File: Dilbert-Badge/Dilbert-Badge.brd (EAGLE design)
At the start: 100 x 80 mm, 5 parts

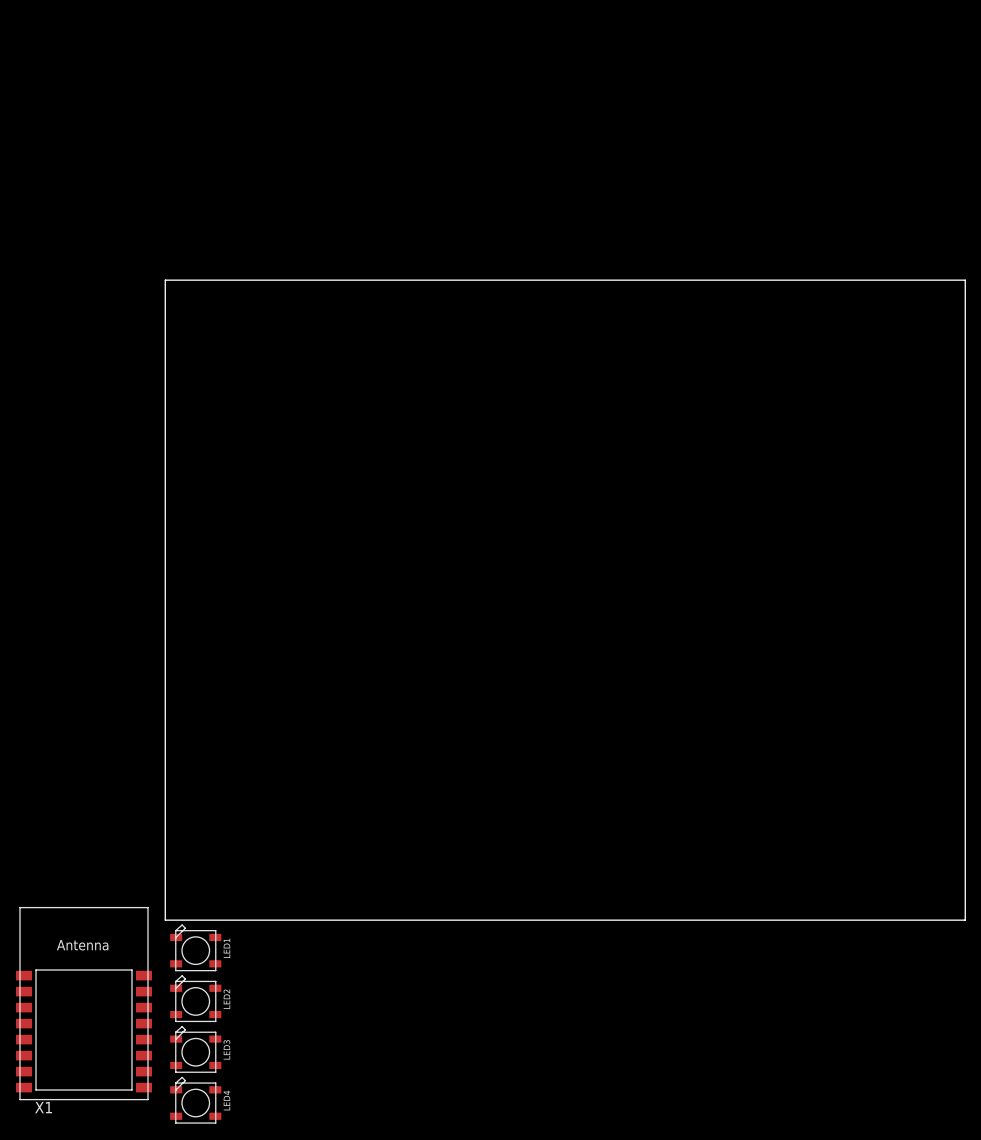
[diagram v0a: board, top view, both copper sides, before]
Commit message: add switches, initial layout
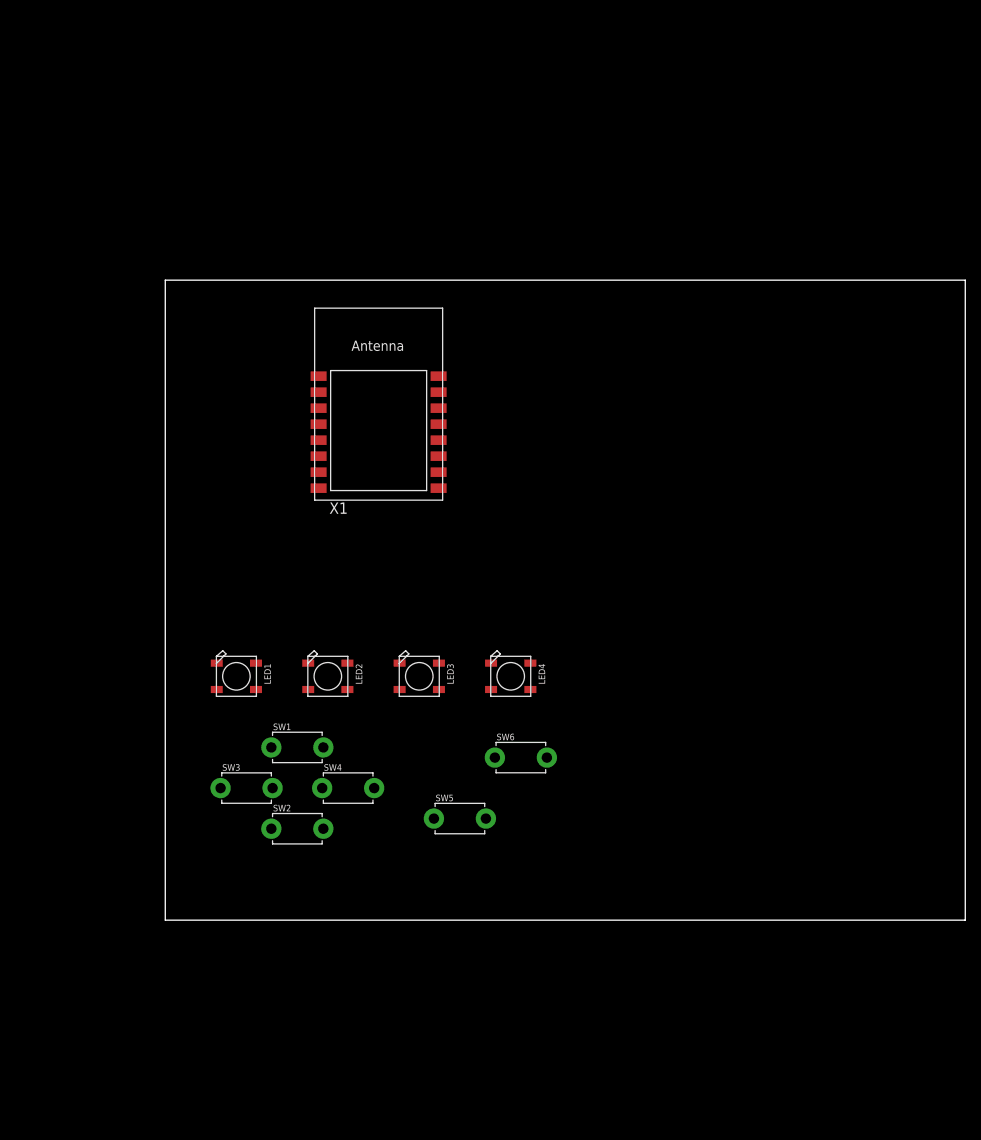
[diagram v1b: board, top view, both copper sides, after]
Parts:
- added SW1: UP, adafruit:TACT_PANA-EVQ
- added SW2: DOWN, adafruit:TACT_PANA-EVQ
- added SW3: LEFT, adafruit:TACT_PANA-EVQ
- added SW4: RIGHT, adafruit:TACT_PANA-EVQ
- added SW5: A, adafruit:TACT_PANA-EVQ
- added SW6: B, adafruit:TACT_PANA-EVQ
- moved X1 83.5 mm to (26.7, 63.5)
- moved LED4 66.3 mm to (43.2, 30.5)
- moved LED3 54.7 mm to (31.8, 30.5)
- moved LED2 43.9 mm to (20.3, 30.5)
- moved LED1 34.7 mm to (8.89, 30.5)
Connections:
- net VCC renamed N$4
- removed net N$6: LED1.3-GND, LED2.3-GND, LED3.3-GND, LED4.3-GND
- new net BTN_A: SW5.P$2
- new net BTN_B: SW6.P$2
- new net BTN_D: SW2.P$2
- new net BTN_L: SW3.P$2
- new net BTN_R: SW4.P$2
- new net BTN_U: SW1.P$2
- net GND: now also LED1.3-GND, LED2.3-GND, LED3.3-GND, LED4.3-GND, SW1.P$1, SW4.P$1, SW5.P$1, SW6.P$1
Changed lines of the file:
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@@
 </autorouter>
 <elements>
-<element name="LED1" library="adafruit" package="WS2812B" value="WS2812B5050" x="3.81" y="-3.81"/>
-<element name="LED2" library="adafruit" package="WS2812B" value="WS2812B5050" x="3.81" y="-10.16"/>
-<element name="LED3" library="adafruit" package="WS2812B" value="WS2812B5050" x="3.81" y="-16.51"/>
-<element name="LED4" library="adafruit" package="WS2812B" value="WS2812B5050" x="3.81" y="-22.86"/>
-<element name="X1" library="adafruit" package="ESP-12" value="" x="-10.16" y="-11.43"/>
+<element name="LED1" library="adafruit" package="WS2812B" value="WS2812B5050" x="8.89" y="30.48"/>
+<element name="LED2" library="adafruit" package="WS2812B" value="WS2812B5050" x="20.32" y="30.48"/>
+<element name="LED3" library="adafruit" package="WS2812B" value="WS2812B5050" x="31.75" y="30.48"/>
+<element name="LED4" library="adafruit" package="WS2812B" value="WS2812B5050" x="43.18" y="30.48"/>
+<element name="X1" library="adafruit" package="ESP-12" value="" x="26.67" y="63.5"/>
+<element name="SW1" library="adafruit" package="TACT_PANA-EVQ" value="UP" x="16.51" y="21.59"/>
+<element name="SW2" library="adafruit" package="TACT_PANA-EVQ" value="DOWN" x="16.51" y="11.43"/>
+<element name="SW3" library="adafruit" package="TACT_PANA-EVQ" value="LEFT" x="10.16" y="16.51"/>
+<element name="SW4" library="adafruit" package="TACT_PANA-EVQ" value="RIGHT" x="22.86" y="16.51"/>
+<element name="SW5" library="adafruit" package="TACT_PANA-EVQ" value="A" x="36.83" y="12.7"/>
+<element name="SW6" library="adafruit" package="TACT_PANA-EVQ" value="B" x="44.45" y="20.32"/>
 </elements>
 <signals>
@@
 <contactref element="LED1" pad="2-DOUT"/>
 <contactref element="LED2" pad="4-DIN"/>
-<wire x1="6.26" y1="-2.16" x2="1.36" y2="-11.81" width="0" layer="19" extent="1-1"/>
+<wire x1="11.34" y1="32.13" x2="17.87" y2="28.83" width="0" layer="19" extent="1-1"/>
 </signal>
 <signal name="N$2">
 <contactref element="LED2" pad="2-DOUT"/>
 <contactref element="LED3" pad="4-DIN"/>
-<wire x1="6.26" y1="-8.51" x2="1.36" y2="-18.16" width="0" layer="19" extent="1-1"/>
+<wire x1="22.77" y1="32.13" x2="29.3" y2="28.83" width="0" layer="19" extent="1-1"/>
 </signal>
 <signal name="N$3">
 <contactref element="LED3" pad="2-DOUT"/>
 <contactref element="LED4" pad="4-DIN"/>
-<wire x1="6.26" y1="-14.86" x2="1.36" y2="-24.51" width="0" layer="19" extent="1-1"/>
+<wire x1="34.2" y1="32.13" x2="40.73" y2="28.83" width="0" layer="19" extent="1-1"/>
 </signal>
 <signal name="N$5">
@@
 <contactref element="LED1" pad="1-VDD"/>
 <contactref element="LED2" pad="1-VDD"/>
-<wire x1="6.26" y1="-18.16" x2="6.26" y2="-24.51" width="0" layer="19" extent="1-1"/>
-<wire x1="6.26" y1="-11.81" x2="6.26" y2="-18.16" width="0" layer="19" extent="1-1"/>
-<wire x1="6.26" y1="-5.46" x2="6.26" y2="-11.81" width="0" layer="19" extent="1-1"/>
+<wire x1="34.2" y1="28.83" x2="45.63" y2="28.83" width="0" layer="19" extent="1-1"/>
+<wire x1="22.77" y1="28.83" x2="34.2" y2="28.83" width="0" layer="19" extent="1-1"/>
+<wire x1="11.34" y1="28.83" x2="22.77" y2="28.83" width="0" layer="19" extent="1-1"/>
 </signal>
-<signal name="N$6">
+<signal name="GND">
+<contactref element="SW1" pad="P$1"/>
+<contactref element="SW4" pad="P$1"/>
+<contactref element="SW5" pad="P$1"/>
+<contactref element="SW6" pad="P$1"/>
 <contactref element="LED1" pad="3-GND"/>
 <contactref element="LED2" pad="3-GND"/>
 <contactref element="LED3" pad="3-GND"/>
 <contactref element="LED4" pad="3-GND"/>
-<wire x1="1.36" y1="-14.86" x2="1.36" y2="-21.21" width="0" layer="19" extent="1-1"/>
-<wire x1="1.36" y1="-8.51" x2="1.36" y2="-14.86" width="0" layer="19" extent="1-1"/>
-<wire x1="1.36" y1="-2.16" x2="1.36" y2="-8.51" width="0" layer="19" extent="1-1"/>
+<contactref element="X1" pad="9"/>
+<wire x1="33.58" y1="12.7" x2="41.2" y2="20.32" width="0" layer="19" extent="1-1"/>
+<wire x1="19.61" y1="16.51" x2="33.58" y2="12.7" width="0" layer="19" extent="1-1"/>
+<wire x1="13.26" y1="21.59" x2="19.61" y2="16.51" width="0" layer="19" extent="1-1"/>
+<wire x1="34.17" y1="54" x2="13.26" y2="21.59" width="0" layer="19" extent="1-1"/>
+<wire x1="40.73" y1="32.13" x2="34.17" y2="54" width="0" layer="19" extent="1-1"/>
+<wire x1="29.3" y1="32.13" x2="40.73" y2="32.13" width="0" layer="19" extent="1-1"/>
+<wire x1="17.87" y1="32.13" x2="29.3" y2="32.13" width="0" layer="19" extent="1-1"/>
+<wire x1="6.44" y1="32.13" x2="17.87" y2="32.13" width="0" layer="19" extent="1-1"/>
 </signal>
-<signal name="VCC">
+<signal name="BTN_U">
+<contactref element="SW1" pad="P$2"/>
+</signal>
+<signal name="BTN_D">
+<contactref element="SW2" pad="P$2"/>
+</signal>
+<signal name="BTN_L">
+<contactref element="SW3" pad="P$2"/>
+</signal>
+<signal name="BTN_R">
+<contactref element="SW4" pad="P$2"/>
+</signal>
+<signal name="BTN_A">
+<contactref element="SW5" pad="P$2"/>
+</signal>
+<signal name="BTN_B">
+<contactref element="SW6" pad="P$2"/>
+</signal>
+<signal name="N$4">
 <contactref element="X1" pad="8"/>
 </signal>
-<signal name="GND">
-<contactref element="X1" pad="9"/>
-</signal>
 </signals>

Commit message: a little more work
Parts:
- added J1: I2C, SparkFun-Connectors:1X04
- added J2: UART, SparkFun-Connectors:1X06
- added J3: (no value), SparkFun-Connectors:1X03
- added J4, J5: (no value), SparkFun-Connectors:1X08_NO_SILK
- added SW7: RESET, adafruit:TACT_PANA-EVQ
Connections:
- new net LED_IN: J5.7, LED1.4-DIN, X1.10
- new net LED_OUT: J3.3, LED4.2-DOUT
- new net N$10: J4.2, X1.7
- new net N$11: J4.3, X1.6
- new net N$12: J5.3, X1.14
- new net N$13: J5.6, X1.11
- new net N$6: J4.6, X1.3
- new net N$7: J4.5, X1.4
- new net N$8: J4.8, X1.1
- new net N$9: J4.4, X1.5
- new net SCL: J1.4, J5.5, X1.12
- new net SDA: J1.3, J5.4, X1.13
- new net UART_CTS: J2.5
- new net UART_DTR: J2.1
- new net UART_RX: J2.3, J5.2, X1.15
- new net UART_TX: J2.2, J5.1, X1.16
- new net VCC: J1.2, J2.4, J3.2, J4.1, X1.8
- net GND: now also J1.1, J2.6, J3.1, J5.8, SW2.P$1, SW3.P$1, SW7.P$1
- net N$4: now also J4.7, X1.2; no longer X1.8
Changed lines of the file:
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@@
 <setting verticaltext="up"/>
 </settings>
-<grid distance="0.05" unitdist="inch" unit="inch" style="lines" multiple="1" display="no" altdistance="0.025" altunitdist="inch" altunit="inch"/>
+<grid distance="0.05" unitdist="inch" unit="inch" style="lines" multiple="1" display="yes" altdistance="0.025" altunitdist="inch" altunit="inch"/>
 <layers>
 <layer number="1" name="Top" color="4" fill="1" visible="yes" active="yes"/>
@@
 <layer number="112" name="tSilk" color="7" fill="1" visible="no" active="yes"/>
 <layer number="113" name="ReferenceLS" color="7" fill="1" visible="no" active="no"/>
+<layer number="114" name="Badge_Outline" color="7" fill="1" visible="yes" active="yes"/>
+<layer number="115" name="ReferenceISLANDS" color="7" fill="1" visible="yes" active="yes"/>
 <layer number="116" name="Patch_BOT" color="9" fill="4" visible="no" active="yes"/>
 <layer number="118" name="Rect_Pads" color="7" fill="1" visible="no" active="no"/>
@@
 <element name="SW5" library="adafruit" package="TACT_PANA-EVQ" value="A" x="36.83" y="12.7"/>
 <element name="SW6" library="adafruit" package="TACT_PANA-EVQ" value="B" x="44.45" y="20.32"/>
+<element name="J1" library="SparkFun-Connectors" package="1X04" value="I2C" x="2.54" y="-3.81">
+<attribute name="PROD_ID" value="CONN-09696" x="2.54" y="-3.81" size="1.778" layer="27" display="off"/>
+</element>
+<element name="J2" library="SparkFun-Connectors" package="1X06" value="UART" x="2.54" y="-8.89">
+<attribute name="PROD_ID" value="CONN-08437" x="2.54" y="-8.89" size="1.778" layer="27" display="off"/>
+</element>
+<element name="J3" library="SparkFun-Connectors" package="1X03" value="" x="2.54" y="-16.51"/>
+<element name="J4" library="SparkFun-Connectors" package="1X08_NO_SILK" value="" x="15.24" y="53.34" rot="R90">
+<attribute name="PROD_ID" value="CONN-08438" x="15.24" y="53.34" size="1.778" layer="27" rot="R90" display="off"/>
+</element>
+<element name="J5" library="SparkFun-Connectors" package="1X08_NO_SILK" value="" x="38.1" y="71.12" rot="R270">
+<attribute name="PROD_ID" value="CONN-08438" x="38.1" y="71.12" size="1.778" layer="27" rot="R270" display="off"/>
+</element>
+<element name="SW7" library="adafruit" package="TACT_PANA-EVQ" value="RESET" x="5.08" y="-21.59"/>
 </elements>
 <signals>
@@
 <contactref element="LED4" pad="3-GND"/>
 <contactref element="X1" pad="9"/>
-<wire x1="33.58" y1="12.7" x2="41.2" y2="20.32" width="0" layer="19" extent="1-1"/>
-<wire x1="19.61" y1="16.51" x2="33.58" y2="12.7" width="0" layer="19" extent="1-1"/>
-<wire x1="13.26" y1="21.59" x2="19.61" y2="16.51" width="0" layer="19" extent="1-1"/>
-<wire x1="34.17" y1="54" x2="13.26" y2="21.59" width="0" layer="19" extent="1-1"/>
-<wire x1="40.73" y1="32.13" x2="34.17" y2="54" width="0" layer="19" extent="1-1"/>
+<contactref element="J2" pad="6"/>
+<contactref element="J1" pad="1"/>
+<contactref element="J3" pad="1"/>
+<contactref element="SW2" pad="P$1"/>
+<contactref element="SW3" pad="P$1"/>
+<contactref element="J5" pad="8"/>
+<contactref element="SW7" pad="P$1"/>
+<wire x1="34.17" y1="54" x2="38.1" y2="53.34" width="0" layer="19" extent="1-1"/>
+<wire x1="40.73" y1="32.13" x2="38.1" y2="53.34" width="0" layer="19" extent="1-1"/>
 <wire x1="29.3" y1="32.13" x2="40.73" y2="32.13" width="0" layer="19" extent="1-1"/>
 <wire x1="17.87" y1="32.13" x2="29.3" y2="32.13" width="0" layer="19" extent="1-1"/>
 <wire x1="6.44" y1="32.13" x2="17.87" y2="32.13" width="0" layer="19" extent="1-1"/>
+<wire x1="13.26" y1="21.59" x2="17.87" y2="32.13" width="0" layer="19" extent="1-1"/>
+<wire x1="19.61" y1="16.51" x2="13.26" y2="21.59" width="0" layer="19" extent="1-1"/>
+<wire x1="13.26" y1="11.43" x2="19.61" y2="16.51" width="0" layer="19" extent="1-1"/>
+<wire x1="6.91" y1="16.51" x2="13.26" y2="21.59" width="0" layer="19" extent="1-1"/>
+<wire x1="41.2" y1="20.32" x2="40.73" y2="32.13" width="0" layer="19" extent="1-1"/>
+<wire x1="33.58" y1="12.7" x2="41.2" y2="20.32" width="0" layer="19" extent="1-1"/>
+<wire x1="2.54" y1="-3.81" x2="13.26" y2="11.43" width="0" layer="19" extent="1-1"/>
+<wire x1="2.54" y1="-16.51" x2="2.54" y2="-3.81" width="0" layer="19" extent="1-1"/>
+<wire x1="1.83" y1="-21.59" x2="2.54" y2="-16.51" width="0" layer="19" extent="1-1"/>
+<wire x1="15.24" y1="-8.89" x2="2.54" y2="-3.81" width="0" layer="19" extent="1-1"/>
 </signal>
 <signal name="BTN_U">
@@
 <contactref element="SW6" pad="P$2"/>
 </signal>
+<signal name="N$8">
+<contactref element="X1" pad="1"/>
+<contactref element="J4" pad="8"/>
+<wire x1="15.24" y1="71.12" x2="19.17" y2="68" width="0" layer="19" extent="1-1"/>
+</signal>
+<signal name="SDA">
+<contactref element="X1" pad="13"/>
+<contactref element="J1" pad="3"/>
+<contactref element="J5" pad="4"/>
+<wire x1="7.62" y1="-3.81" x2="34.17" y2="62" width="0" layer="19" extent="1-1"/>
+<wire x1="38.1" y1="63.5" x2="7.62" y2="-3.81" width="0" layer="19" extent="1-1"/>
+</signal>
+<signal name="SCL">
+<contactref element="X1" pad="12"/>
+<contactref element="J1" pad="4"/>
+<contactref element="J5" pad="5"/>
+<wire x1="10.16" y1="-3.81" x2="34.17" y2="60" width="0" layer="19" extent="1-1"/>
+<wire x1="38.1" y1="60.96" x2="10.16" y2="-3.81" width="0" layer="19" extent="1-1"/>
+</signal>
+<signal name="UART_TX">
+<contactref element="X1" pad="16"/>
+<contactref element="J2" pad="2"/>
+<contactref element="J5" pad="1"/>
+<wire x1="5.08" y1="-8.89" x2="34.17" y2="68" width="0" layer="19" extent="1-1"/>
+<wire x1="38.1" y1="71.12" x2="5.08" y2="-8.89" width="0" layer="19" extent="1-1"/>
+</signal>
+<signal name="UART_RX">
+<contactref element="X1" pad="15"/>
+<contactref element="J2" pad="3"/>
+<contactref element="J5" pad="2"/>
+<wire x1="7.62" y1="-8.89" x2="34.17" y2="66" width="0" layer="19" extent="1-1"/>
+<wire x1="38.1" y1="68.58" x2="7.62" y2="-8.89" width="0" layer="19" extent="1-1"/>
+</signal>
+<signal name="UART_CTS">
+<contactref element="J2" pad="5"/>
+</signal>
+<signal name="VCC">
+<contactref element="J2" pad="4"/>
+<contactref element="X1" pad="8"/>
+<contactref element="J3" pad="2"/>
+<contactref element="J1" pad="2"/>
+<contactref element="J4" pad="1"/>
+<wire x1="5.08" y1="-3.81" x2="19.17" y2="54" width="0" layer="19" extent="1-1"/>
+<wire x1="10.16" y1="-8.89" x2="5.08" y2="-3.81" width="0" layer="19" extent="1-1"/>
+<wire x1="5.08" y1="-16.51" x2="10.16" y2="-8.89" width="0" layer="19" extent="1-1"/>
+<wire x1="15.24" y1="53.34" x2="5.08" y2="-16.51" width="0" layer="19" extent="1-1"/>
+</signal>
+<signal name="UART_DTR">
+<contactref element="J2" pad="1"/>
+</signal>
+<signal name="LED_OUT">
+<contactref element="LED4" pad="2-DOUT"/>
+<contactref element="J3" pad="3"/>
+<wire x1="7.62" y1="-16.51" x2="45.63" y2="32.13" width="0" layer="19" extent="1-1"/>
+</signal>
+<signal name="LED_IN">
+<contactref element="LED1" pad="4-DIN"/>
+<contactref element="X1" pad="10"/>
+<contactref element="J5" pad="7"/>
+<wire x1="6.44" y1="28.83" x2="34.17" y2="56" width="0" layer="19" extent="1-1"/>
+<wire x1="38.1" y1="55.88" x2="6.44" y2="28.83" width="0" layer="19" extent="1-1"/>
+</signal>
 <signal name="N$4">
-<contactref element="X1" pad="8"/>
+<contactref element="X1" pad="2"/>
+<contactref element="J4" pad="7"/>
+<wire x1="15.24" y1="68.58" x2="19.17" y2="66" width="0" layer="19" extent="1-1"/>
+</signal>
+<signal name="N$6">
+<contactref element="J4" pad="6"/>
+<contactref element="X1" pad="3"/>
+<wire x1="15.24" y1="66.04" x2="19.17" y2="64" width="0" layer="19" extent="1-1"/>
+</signal>
+<signal name="N$7">
+<contactref element="X1" pad="4"/>
+<contactref element="J4" pad="5"/>
+<wire x1="15.24" y1="63.5" x2="19.17" y2="62" width="0" layer="19" extent="1-1"/>
+</signal>
+<signal name="N$9">
+<contactref element="J4" pad="4"/>
+<contactref element="X1" pad="5"/>
+<wire x1="15.24" y1="60.96" x2="19.17" y2="60" width="0" layer="19" extent="1-1"/>
+</signal>
+<signal name="N$10">
+<contactref element="J4" pad="2"/>
+<contactref element="X1" pad="7"/>
+<wire x1="15.24" y1="55.88" x2="19.17" y2="56" width="0" layer="19" extent="1-1"/>
+</signal>
+<signal name="N$11">
+<contactref element="X1" pad="6"/>
+<contactref element="J4" pad="3"/>
+<wire x1="15.24" y1="58.42" x2="19.17" y2="58" width="0" layer="19" extent="1-1"/>
+</signal>
+<signal name="N$12">
+<contactref element="X1" pad="14"/>
+<contactref element="J5" pad="3"/>
+<wire x1="38.1" y1="66.04" x2="34.17" y2="64" width="0" layer="19" extent="1-1"/>
+</signal>
+<signal name="N$13">
+<contactref element="J5" pad="6"/>
+<contactref element="X1" pad="11"/>
+<wire x1="38.1" y1="58.42" x2="34.17" y2="58" width="0" layer="19" extent="1-1"/>
 </signal>
 </signals>
